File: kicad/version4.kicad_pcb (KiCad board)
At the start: 2 copper layers, 49.5 x 33 mm, 19 parts, among them J1 valve out, J2 12V in, J3 sense, U1 stepdown, U2 WeMos_mini, U3 DS18B20

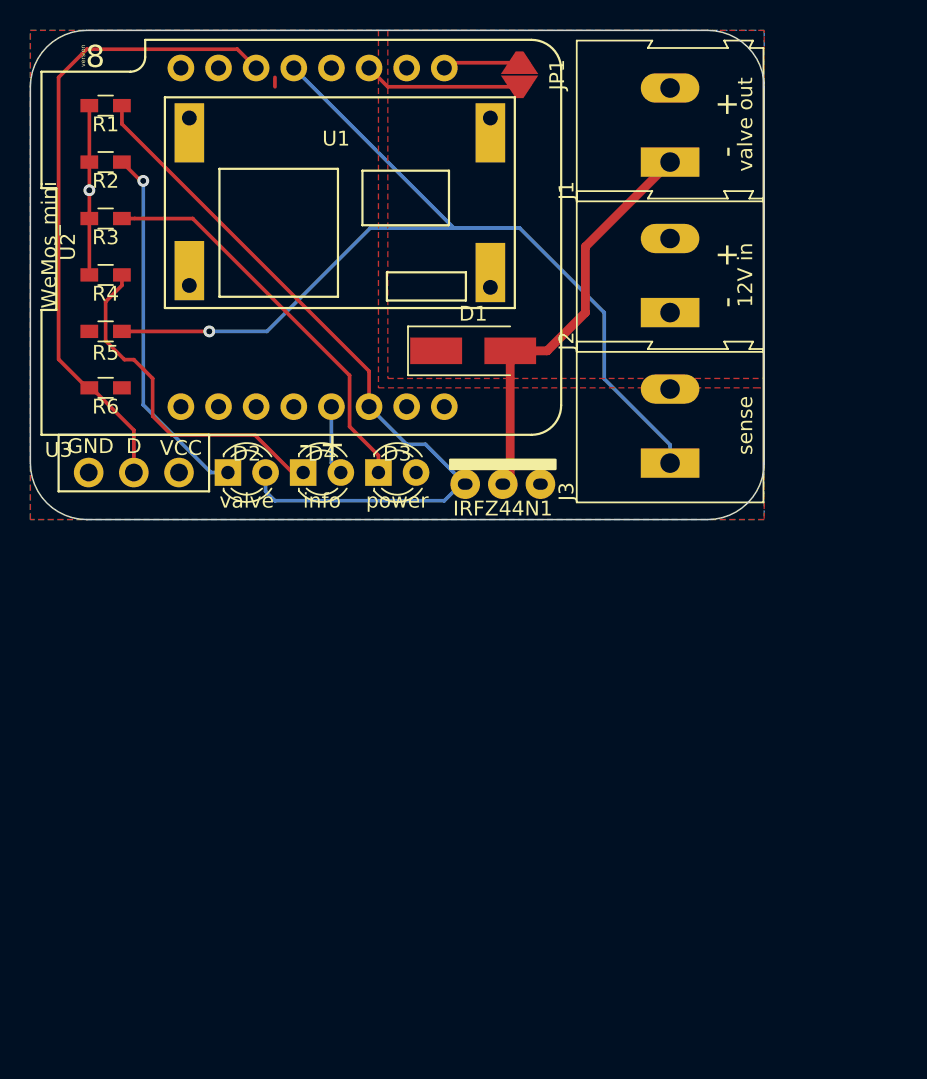
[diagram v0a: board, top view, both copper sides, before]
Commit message: cleaned up old files and replaced main pcb with smd version
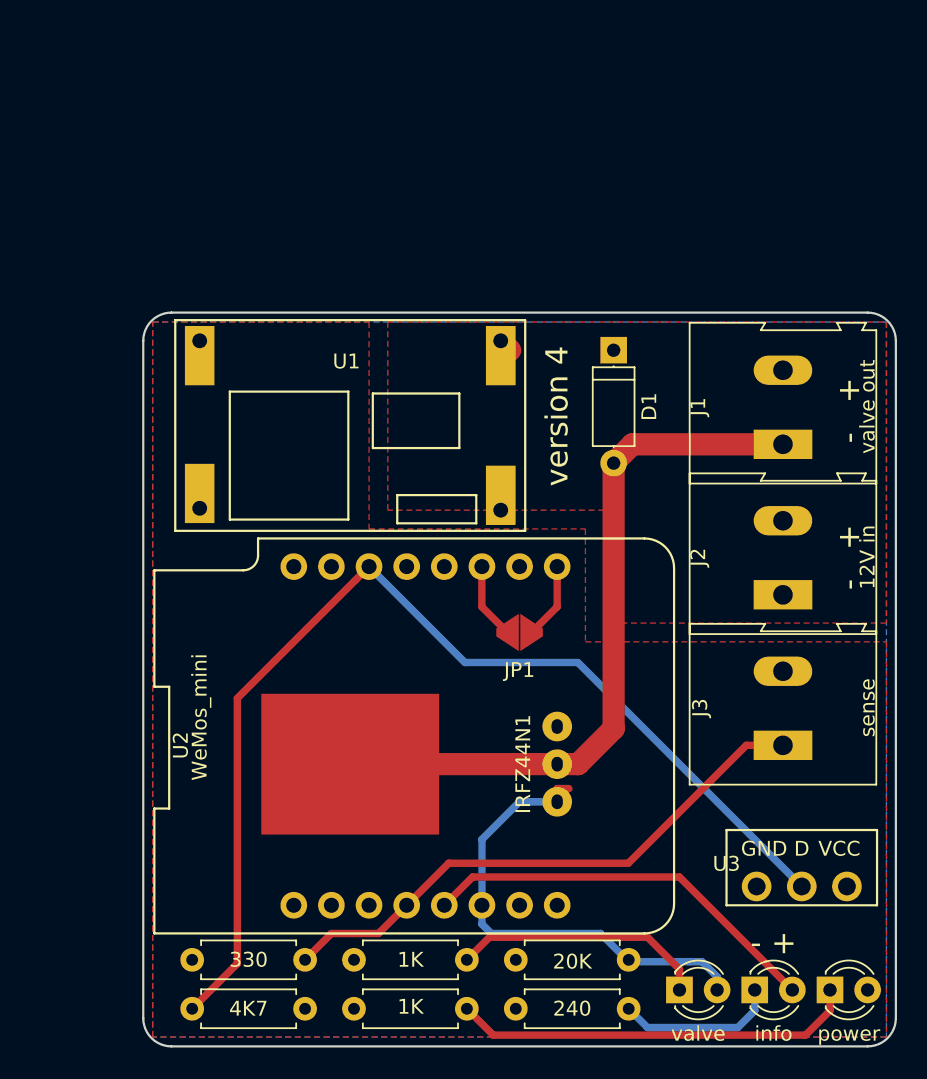
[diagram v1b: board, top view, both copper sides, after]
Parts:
- removed ?: , 
- D1: footprint Diodes_SMD:D_SMA_Handsoldering -> Diodes_THT:D_A-405_P7.62mm_Horizontal
- D3: value LED -> power
- IRFZ44N1: footprint custom:irlz44n_vertical -> custom:irlz44n
- R1, R2, R3, R4, R5, R6: footprint Resistors_SMD:R_0603_HandSoldering -> Resistors_THT:R_Axial_DIN0207_L6.3mm_D2.5mm_P7.62mm_Horizontal
- moved R1 64.0 mm to (150.9, 102.1)
- moved R3 58.6 mm to (147.6, 105.4)
- moved R4 56.7 mm to (150.9, 105.4)
- moved R2 56.4 mm to (140.0, 102.1)
- moved U3 53.0 mm to (170.2, 99.7)
- moved D2 46.4 mm to (161.9, 104.1)
- moved D3 46.4 mm to (172.1, 104.1)
- moved D4 46.4 mm to (167.0, 104.1)
- moved R5 44.5 mm to (136.7, 102.1)
- moved R6 44.0 mm to (136.7, 105.4)
- moved JP1 37.6 mm to (151.1, 80.0), turned to 0 degrees
- moved U2 34.5 mm to (144.8, 87.0)
- moved J1 20.5 mm to (168.9, 67.3)
- moved J2 20.5 mm to (168.9, 77.5)
- moved J3 20.5 mm to (168.9, 87.6)
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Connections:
- U2 pad 13: Net-(J3-Pad1) -> Net-(U2-Pad13)
- U2 pad 4: Net-(U2-Pad4) -> Net-(J3-Pad1)
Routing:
- net Net-(R6-Pad2): track 43.6 -> 72.9 mm
- net Net-(J3-Pad1): track 65.1 -> 38.3 mm, vias 1 -> 0
- net Net-(D4-Pad2): track 4.71 -> 27.4 mm
- net Net-(D1-Pad2): track 27.9 -> 48.7 mm
- net Net-(D2-Pad2): track 51.1 -> 32.4 mm
- net Net-(D4-Pad1): track 23.4 -> 10.9 mm
- net GND: track 11.4 -> 3.81 mm, vias 1 -> 0
- net Net-(D2-Pad1): track 24.5 -> 17.3 mm, vias 1 -> 0
- net Net-(JP1-Pad1): track 10.7 -> 5.16 mm
- net +12V: track 0.00 -> 3.52 mm
- net +3V3: track 0.88 -> 1.90 mm
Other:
- board size 49.5 x 33 mm -> 50.8 x 49.5 mm
- net class Default: trace_width 0.25 -> 0.5; via_dia 0.8 -> 0.6
- net class more removed
- net class power added: clearance 0.4, trace_width 1.5, via_dia 0.6, via_drill 0.4
- rule pad_to_mask_clearance: 0 -> 0.2
- board text added: "4"
- board text added: "made by humans on earth"
- board text added: "version 4"
- board text removed: "8"
- board text removed: "info"
- board text removed: "power"
- board text removed: "valve"
- board text removed: "version"
